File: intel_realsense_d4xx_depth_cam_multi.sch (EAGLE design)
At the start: 6 parts, among them SW1 300mA/4V

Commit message: Rev 1: Board complete.
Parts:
- removed U$2, U$3: SM09B-SRSS-TB, PiB_connectors:1X09_SM09B-SRSS-TB
- added CAM2, CAM3: SM09B-SRSS-TB, PiB_connectors:1X09_SM09B-SRSS-TB
- renumbered U$1 to CAM1
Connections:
- net GND: now also CAM2.9, CAM3.9; no longer U$2.9, U$3.9
- net SYNC: now also CAM2.5, CAM3.5; no longer U$2.5, U$3.5
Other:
- moved on the sheet: BNC1, S1, SW1

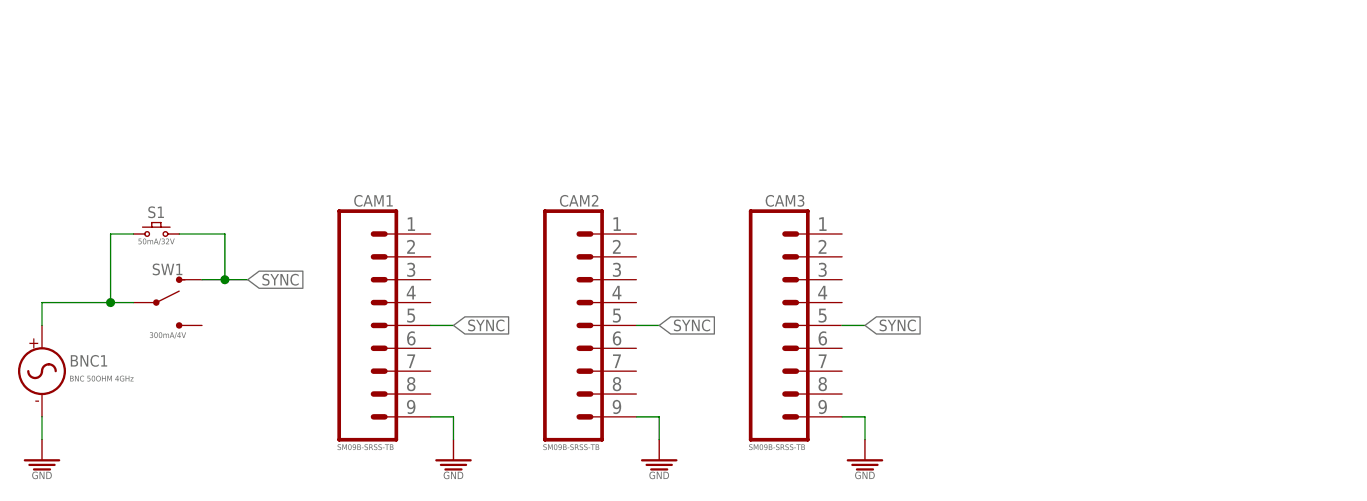
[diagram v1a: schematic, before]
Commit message: Add 22nF cap and 20K resistor.
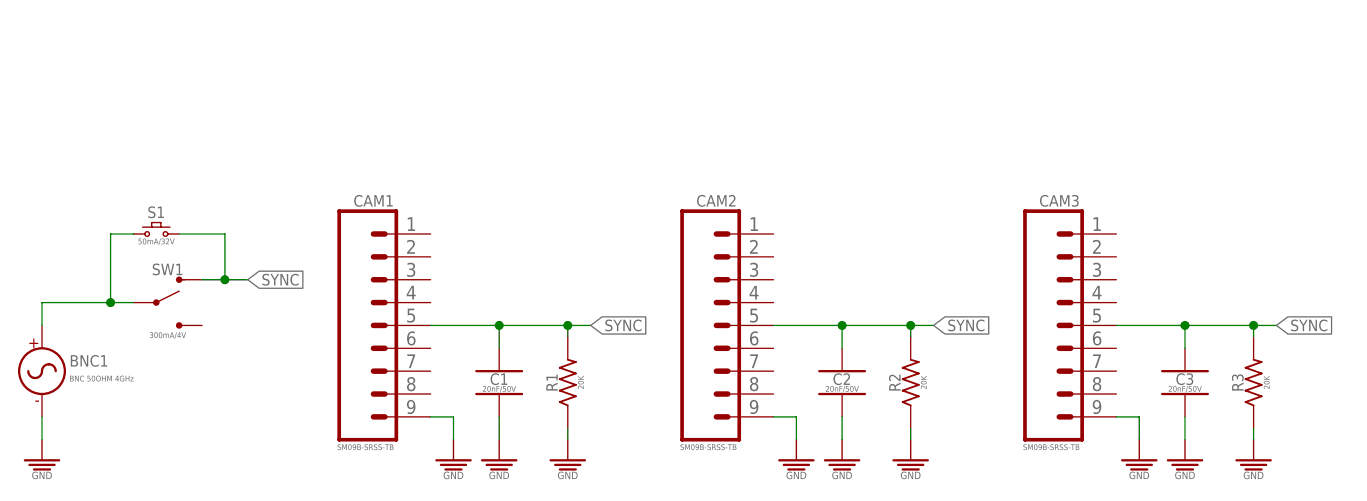
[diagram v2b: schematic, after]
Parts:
- added C1, C2, C3: 20nF/50V, PiB_capacitors:22NF_CER_SMD-0603_50V-10%
- added R1, R2, R3: 20K, PiB_resistors:20KΩ_SMD-0603_1/10W-5%
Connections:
- net GND: now also C1.2, C2.2, C3.2, R1.1, R2.1, R3.1
- net SYNC: now also C1.1, C2.1, C3.1, R1.2, R2.2, R3.2
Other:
- moved on the sheet: CAM2, CAM3

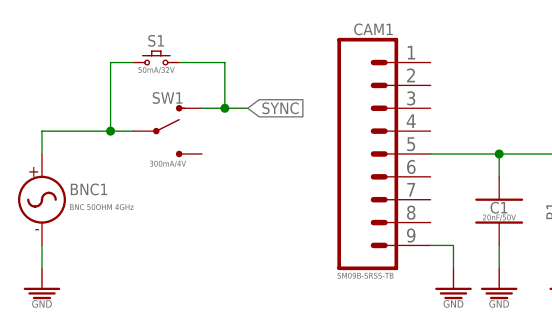
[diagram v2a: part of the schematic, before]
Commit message: Add BOM for intel depth cam.
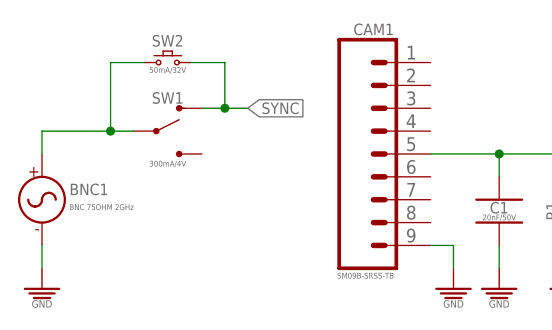
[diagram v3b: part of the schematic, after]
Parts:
- removed S1: 50mA/32V, PiB_switches:SWITCH_MOMENTARY_SPST-NO_SMD_50MA-32V_L4.6-W2.8
- added SW2: 50mA/32V, PiB_switches:SWITCH_MOMENTARY_SPST-NO_SMD_50MA-32V_L4.6-W2.8
- BNC1: value BNC 50OHM 4GHz -> BNC 75OHM 2GHz; device PiB_connectors:BNC_CONNECTOR_PTH_50OHM_4GHZ -> PiB_connectors:BNC_CONNECTOR_PTH_75OHM_2GHZ
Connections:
- net N$1: now also SW2.1; no longer S1.1
- net SYNC: now also SW2.2; no longer S1.2
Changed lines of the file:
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@@
 <setting verticaltext="up"/>
 </settings>
-<grid distance="0.1" unitdist="inch" unit="inch" style="lines" multiple="1" display="no" altdistance="0.05" altunitdist="inch" altunit="inch"/>
+<grid distance="0.1" unitdist="inch" unit="inch" style="lines" multiple="1" display="yes" altdistance="0.05" altunitdist="inch" altunit="inch"/>
 <layers>
 <layer number="1" name="Top" color="4" fill="1" visible="no" active="no"/>
@@
 <part name="CAM2" library="PiB_connectors" library_urn="urn:adsk.eagle:library:6338520" deviceset="1X09" device="_SM09B-SRSS-TB" package3d_urn="urn:adsk.eagle:package:6338575/1" value="SM09B-SRSS-TB"/>
 <part name="CAM3" library="PiB_connectors" library_urn="urn:adsk.eagle:library:6338520" deviceset="1X09" device="_SM09B-SRSS-TB" package3d_urn="urn:adsk.eagle:package:6338575/1" value="SM09B-SRSS-TB"/>
-<part name="BNC1" library="PiB_connectors" deviceset="BNC_CONNECTOR" device="_PTH_50OHM_4GHZ" package3d_urn="urn:adsk.eagle:package:6338576/2" value="BNC 50OHM 4GHz"/>
+<part name="BNC1" library="PiB_connectors" deviceset="BNC_CONNECTOR" device="_PTH_75OHM_2GHZ" package3d_urn="urn:adsk.eagle:package:6338576/2" value="BNC 75OHM 2GHz"/>
 <part name="SUPPLY1" library="PiB_power_symbols" deviceset="GND" device=""/>
 <part name="SUPPLY2" library="PiB_power_symbols" deviceset="GND" device=""/>
@@
 <part name="SUPPLY4" library="PiB_power_symbols" deviceset="GND" device=""/>
 <part name="SW1" library="PiB_switches" deviceset="SWITCH_SPDT" device="_RA_SMD_300MA-4V_6.7L-2.6W" package3d_urn="urn:adsk.eagle:package:2959400/3" value="300mA/4V"/>
-<part name="S1" library="PiB_switches" deviceset="SWITCH_MOMENTARY" device="_SPST-NO_SMD_50MA-32V_L4.6-W2.8" package3d_urn="urn:adsk.eagle:package:3034784/2" value="50mA/32V"/>
+<part name="SW2" library="PiB_switches" deviceset="SWITCH_MOMENTARY" device="_SPST-NO_SMD_50MA-32V_L4.6-W2.8" package3d_urn="urn:adsk.eagle:package:3034784/2" value="50mA/32V"/>
 <part name="R1" library="PiB_resistors" deviceset="20KΩ" device="_SMD-0603_1/10W-5%" package3d_urn="urn:adsk.eagle:package:2959474/1" value="20K"/>
 <part name="C1" library="PiB_capacitors" deviceset="22NF" device="_CER_SMD-0603_50V-10%" package3d_urn="urn:adsk.eagle:package:3041595/1" value="20nF/50V"/>
@@
 <attribute name="VALUE" x="-6.35" y="37.338" size="0.635" layer="96" font="vector" ratio="10" align="top-center"/>
 </instance>
-<instance part="S1" gate="G$1" x="-7.62" y="48.26" smashed="yes">
-<attribute name="NAME" x="-7.62" y="50.038" size="1.27" layer="95" font="vector" ratio="10" align="bottom-center"/>
-<attribute name="VALUE" x="-7.62" y="47.752" size="0.635" layer="96" font="vector" ratio="10" align="top-center"/>
+<instance part="SW2" gate="G$1" x="-6.35" y="48.26" smashed="yes">
+<attribute name="NAME" x="-6.35" y="50.038" size="1.27" layer="95" font="vector" ratio="10" align="bottom-center"/>
+<attribute name="VALUE" x="-6.35" y="47.752" size="0.635" layer="96" font="vector" ratio="10" align="top-center"/>
 </instance>
 <instance part="R1" gate="G$1" x="38.1" y="31.75" smashed="yes" rot="R90">
@@
 <wire x1="2.54" y1="43.18" x2="0" y2="43.18" width="0.1524" layer="91"/>
 <label x="2.54" y="43.18" size="1.27" layer="95" font="vector" ratio="10" xref="yes"/>
-<pinref part="S1" gate="G$1" pin="2"/>
+<pinref part="SW2" gate="G$1" pin="2"/>
 <wire x1="0" y1="43.18" x2="-2.54" y2="43.18" width="0.1524" layer="91"/>
-<wire x1="-5.08" y1="48.26" x2="0" y2="48.26" width="0.1524" layer="91"/>
+<wire x1="-3.81" y1="48.26" x2="0" y2="48.26" width="0.1524" layer="91"/>
 <wire x1="0" y1="48.26" x2="0" y2="43.18" width="0.1524" layer="91"/>
 <junction x="0" y="43.18"/>
@@
 <wire x1="-20.32" y1="38.1" x2="-20.32" y2="40.64" width="0.1524" layer="91"/>
 <wire x1="-20.32" y1="40.64" x2="-12.7" y2="40.64" width="0.1524" layer="91"/>
-<pinref part="S1" gate="G$1" pin="1"/>
+<pinref part="SW2" gate="G$1" pin="1"/>
 <wire x1="-12.7" y1="40.64" x2="-10.16" y2="40.64" width="0.1524" layer="91"/>
-<wire x1="-10.16" y1="48.26" x2="-12.7" y2="48.26" width="0.1524" layer="91"/>
+<wire x1="-8.89" y1="48.26" x2="-12.7" y2="48.26" width="0.1524" layer="91"/>
 <wire x1="-12.7" y1="48.26" x2="-12.7" y2="40.64" width="0.1524" layer="91"/>
 <junction x="-12.7" y="40.64"/>
